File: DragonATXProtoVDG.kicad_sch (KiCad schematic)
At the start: 67 parts, among them IC1 74LS273, IC2 MC6847, IC3 MC14053, J3 JTAG, Q1 MMBT4401, Q2 NPN, Q3 NPN, Q4 NPN, Q5 NPN, Q6 NPN, U1 AD724JR, U3 ATF1502ASL-xAx44, Y2 4.433618MHz

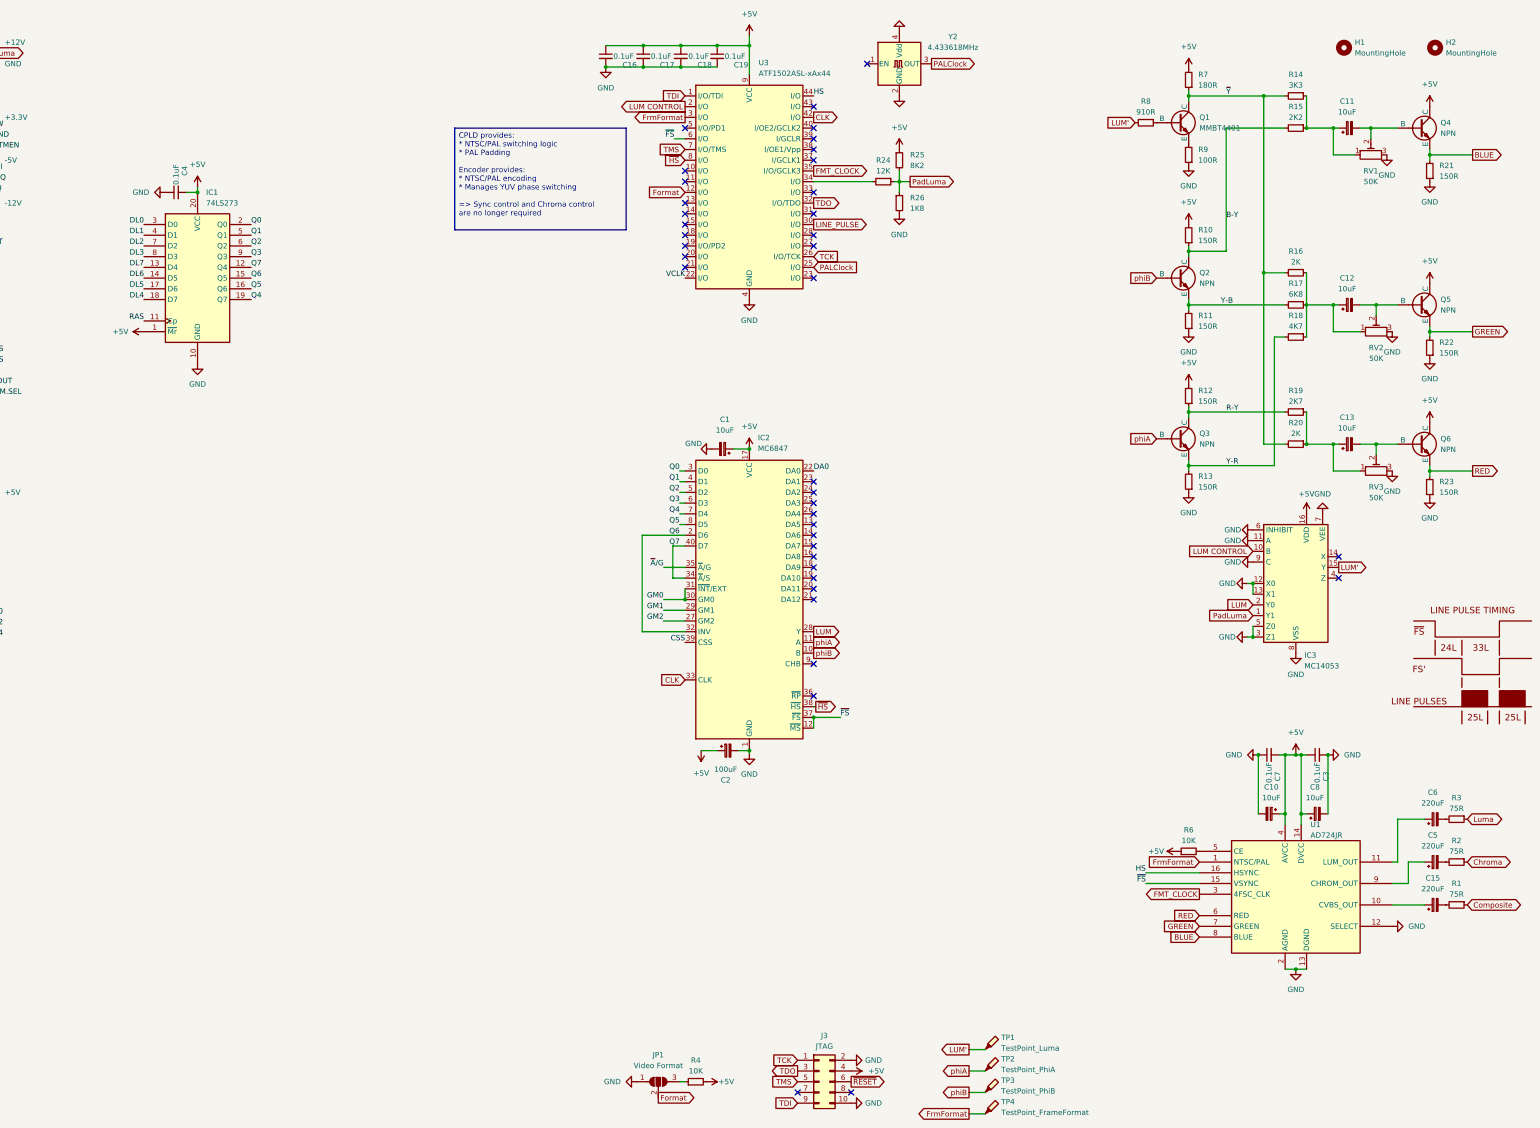
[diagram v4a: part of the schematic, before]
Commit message: fix luma attenuation
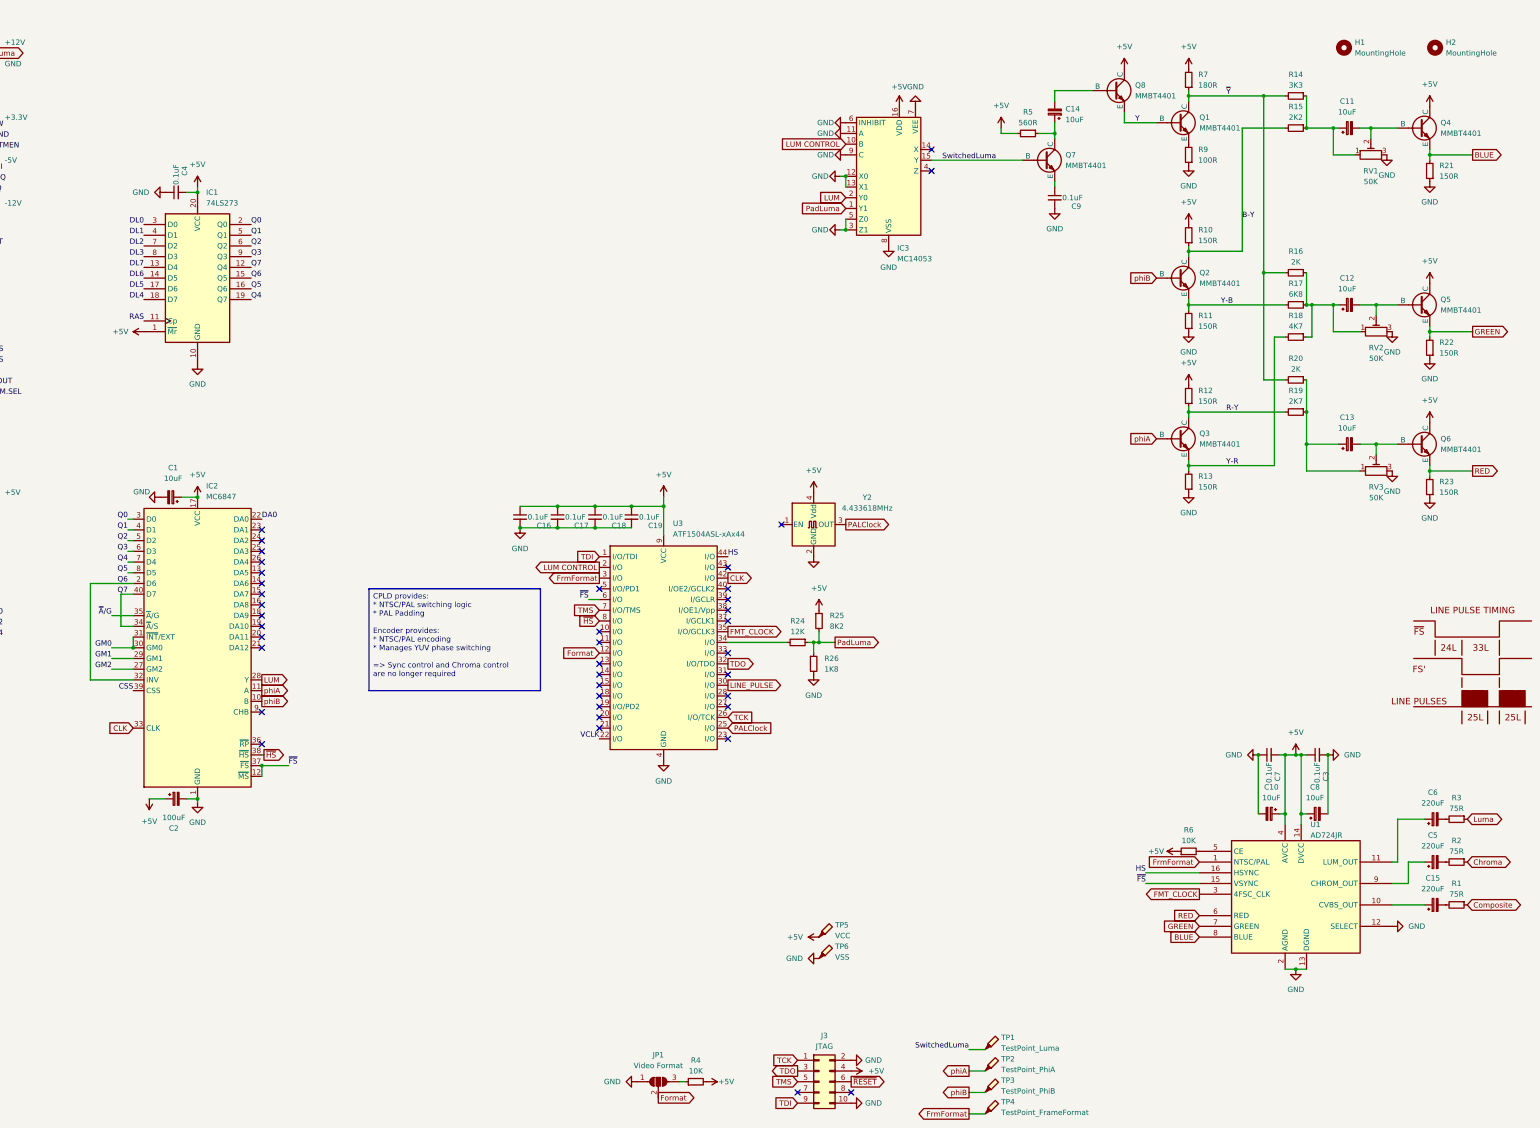
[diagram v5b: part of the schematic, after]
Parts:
- removed R8: 910R, Resistor_SMD:R_0805_2012Metric_Pad1.20x1.40mm_HandSolder, symbol Device:R_Small
- added C14: 10uF, Capacitor_SMD:CP_Elec_4x5.4, symbol Device:C_Polarized_Small
- added C9: 0.1uF, Capacitor_SMD:C_0805_2012Metric_Pad1.18x1.45mm_HandSolder, symbol Device:C_Small
- added Q7, Q8: MMBT4401, Library:SOT-23-3, symbol Simulation_SPICE:NPN
- added R5: 560R, Resistor_SMD:R_0805_2012Metric_Pad1.20x1.40mm_HandSolder, symbol Device:R_Small
- added TP5: VCC, TestPoint:TestPoint_Loop_D3.80mm_Drill2.0mm, symbol Connector:TestPoint_Probe
- added TP6: VSS, TestPoint:TestPoint_Loop_D3.80mm_Drill2.0mm, symbol Connector:TestPoint_Probe
- C1, C10, C11, C12, C13, C8: LCSC (none) -> C3343
- C15, C5, C6: footprint Capacitor_Tantalum_SMD:CP_EIA-3216-12_Kemet-S -> Capacitor_Tantalum_SMD:CP_EIA-3528-12_Kemet-T_HandSolder; LCSC (none) -> C7200
- C16, C17, C18, C19, C3, C4, C7: LCSC (none) -> C1711
- C2: LCSC (none) -> C3338
- IC1: LCSC (none) -> C206102
- IC3: LCSC (none) -> C6742
- PL1, TP1, TP2, TP3, TP4: now left out of the parts list
- Q1: LCSC (none) -> C31776
- Q2, Q3, Q4, Q5, Q6: value NPN -> MMBT4401; LCSC (none) -> C31776
- R1, R2, R3: LCSC (none) -> C17820
- R10, R11, R12, R13: LCSC (none) -> C17471
- R14: LCSC (none) -> C26010
- R15: LCSC (none) -> C17520
- R16, R20: LCSC (none) -> C17604
- R17: LCSC (none) -> C17772
- R18: LCSC (none) -> C17673
- R19: LCSC (none) -> C17530
- R21, R22, R23: LCSC (none) -> C22808
- R24: LCSC (none) -> C17444
- R25: LCSC (none) -> C17828
- R26: LCSC (none) -> C17398
- R4, R6: LCSC (none) -> C17414
- R7: LCSC (none) -> C25270
- R9: LCSC (none) -> C17408
- RV1, RV2, RV3: LCSC (none) -> C913246
- U3: value ATF1502ASL-xAx44 -> ATF1504ASL-xAx44
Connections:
- net +5V: now also Y2.4 (Vdd), Q8.1 (C), R5.2, TP5.1
- net GND: now also C9.2, TP6.1; no longer Y2.4 (Vdd)
- net Y: now reaches Q1.2 (B)
- net Y: now also Q8.3 (E)
- net LUM' renamed SwitchedLuma
- net SwitchedLuma: now also Q7.2 (B)
- new net: C14.1, Q7.1 (C), R5.1
- new net: C9.1, Q7.3 (E)
- new net: C14.2, Q8.2 (B)
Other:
- moved on the sheet: C1, C16, C17, C18, C19, C2, IC2, IC3, R20, R24, R25, R26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
